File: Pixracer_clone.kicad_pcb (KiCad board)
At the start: 4 copper layers, 47.5 x 47.5 mm, 98 parts, among them J1 Conn_01x03_Male, J10 Conn_01x04_Male, J11 Conn_01x04_Male, J12 Conn_01x04_Male, J13 Conn_01x04_Male, J14 UART4_con, J15 UART4_con, J16 UART4_con, J17 Conn_01x06_Male, J18 Micro_SD_Card, J2 USB_B_Micro, J20 Conn_01x04_Male, J3 Conn_01x08_Male, J4 Conn_01x08_Male, J5 Conn_01x08_Male, J6 Conn_01x02_Male, J7 Conn_01x03_Male, J8 Conn_01x02_Male, J9 UART4_con, Q1 2N3904, Q2 2N3904, SW1 SW_Push, U1 STM32F427VITx, U10 LP5907MFX-3.3, U11 NRF24L01_Breakout, U2 USBLC6-2SC6, U3 ICM-20948, U4 MPU-9250, U5 LSM6DS3, U6 TJA1051T, U7 LP5907MFX-1.8, U8 LP5907MFX-3.3, U9 25LCxxx, Y1 Crystal_GND24

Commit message: finish board
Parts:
- removed C11: 1u, Capacitor_SMD:C_0402_1005Metric
- removed C22: CP, Capacitor_SMD:C_1206_3216Metric
- removed C32: 1uF, Capacitor_SMD:C_0402_1005Metric
- removed C33: 100nF, Capacitor_SMD:C_0402_1005Metric
- removed C41: C, Capacitor_SMD:C_0603_1608Metric
- removed F1: Fuse, Fuse:Fuse_1812_4532Metric
- removed J13: Conn_01x04_Male, Connector_PinHeader_2.54mm:PinHeader_1x04_P2.54mm_Vertical
- removed J9: UART4_con, Connector_PinHeader_2.54mm:PinHeader_1x04_P2.54mm_Vertical
- added C25: CP, Capacitor_SMD:C_1206_3216Metric, F.Cu at (179.1, 112.7)
- added C43: 1uF, Capacitor_SMD:C_0603_1608Metric_Pad1.05x0.95mm_HandSolder, F.Cu at (147.8, 85.1)
- added J19: Conn_01x02_Male, Connector_PinHeader_2.54mm:PinHeader_1x02_P2.54mm_Vertical, F.Cu at (189.6, 88.2)
- added J21: Conn_01x06_Male, Connector_JST:JST_SH_SM06B-SRSS-TB_1x06-1MP_P1.00mm_Horizontal, B.Cu at (147.1, 82.0)
- added J22: Conn_01x06_Male, Connector_JST:JST_SH_SM06B-SRSS-TB_1x06-1MP_P1.00mm_Horizontal, F.Cu at (147.5, 112.7)
- added J23: Conn_01x10_Male, Connector_PinHeader_2.54mm:PinHeader_1x10_P2.54mm_Vertical, F.Cu at (157.6, 120.1)
- added R4: 22R, Resistor_SMD:R_0603_1608Metric_Pad1.05x0.95mm_HandSolder, F.Cu at (185.9, 82.9)
- C15: value C -> 1uF; footprint Capacitor_SMD:C_0603_1608Metric -> Capacitor_SMD:C_0603_1608Metric_Pad1.05x0.95mm_HandSolder
- C39, D2, J8, Q1, R2: moved to B.Cu
- C7, J15, R5, R6, Rc_sbus1: moved to F.Cu
- J14: footprint Connector_JST:JST_SH_BM04B-SRSS-TB_1x04-1MP_P1.00mm_Vertical -> Connector_JST:JST_SH_SM04B-SRSS-TB_1x04-1MP_P1.00mm_Horizontal
- J6: value Conn_01x02_Male -> Conn_01x04_Male; footprint Connector_PinHeader_2.54mm:PinHeader_1x02_P2.54mm_Vertical -> Connector_JST:JST_SH_SM04B-SRSS-TB_1x04-1MP_P1.00mm_Horizontal
- J7: value Conn_01x03_Male -> Conn_01x04_Male; footprint Connector_JST:JST_SH_BM03B-SRSS-TB_1x03-1MP_P1.00mm_Vertical -> Connector_JST:JST_SH_SM04B-SRSS-TB_1x04-1MP_P1.00mm_Horizontal
- R3: value R -> 22R; footprint Resistor_SMD:R_0402_1005Metric -> Resistor_SMD:R_0603_1608Metric_Pad1.05x0.95mm_HandSolder
- U2: value USBLC6-2SC6 -> LP5907MFX-3.3; footprint Package_TO_SOT_SMD:SOT-23-6 -> Package_TO_SOT_SMD:SOT-23-5
- moved C15 67.0 mm to (153.2, 85.1), turned to 90 degrees
- moved R3 55.7 mm to (185.9, 81.2), turned to 180 degrees
- moved C12 48.5 mm to (157.5, 99.4), turned to 90 degrees
- moved C30 41.9 mm to (185.2, 112.7), turned to 90 degrees
- moved J8 39.6 mm to (186.2, 75.8), turned to 90 degrees
- moved C10 39.5 mm to (157.3, 95.6), turned to 90 degrees
- moved C6 39.0 mm to (156.4, 91.8), turned to 90 degrees
- moved Rc_sbus1 38.4 mm to (156.3, 106.9)
- moved J16 35.0 mm to (190.7, 113.9), turned to 90 degrees
- moved U2 34.8 mm to (150.5, 85.2)
- moved R6 32.8 mm to (156.3, 111.1)
- moved Q1 31.8 mm to (184.0, 79.3)
- moved R2 31.6 mm to (187.7, 79.4)
- moved R5 29.8 mm to (156.3, 112.6), turned to 180 degrees
- moved J6 29.4 mm to (162.2, 75.4), turned to 180 degrees
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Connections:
- C15 pad 1: VBUS -> +5V
- C21 pad 1: 5V_IN -> +5V
- C30 pad 1: 5V_IN -> +5V
- D2 pad 1: 5V_IN -> +5V
- J10 pad 2: UART1_RX -> UART1_TX
- J10 pad 3: UART1_TX -> UART1_RX
- J10 pad 4: VCC -> +5V
- J11 pad 4: VCC -> +3V3
- J12 pad 4: VCC -> +5V
- J14 pad 2: I2C_SDA -> I2C_SCl
- J14 pad 3: I2C_SCl -> I2C_SDA
- J14 pad 4: 5V_IN -> +5V
- J15 pad 2: I2C2_SDA -> I2C2_SCl
- J15 pad 3: I2C2_SCl -> I2C2_SDA
- J15 pad 4: 5V_IN -> +5V
- J16 pad 1: VCC -> +5V
- J17 pad 1: VCC -> +5V
- J20 pad 4: 5V_IN -> +5V
- J5 pad 1: 5V_IN -> +5V
- J5 pad 2: 5V_IN -> +5V
- J5 pad 3: 5V_IN -> +5V
- J5 pad 4: 5V_IN -> +5V
- J5 pad 5: 5V_IN -> +5V
- J5 pad 6: 5V_IN -> +5V
- J5 pad 7: 5V_IN -> +5V
- J5 pad 8: 5V_IN -> +5V
- J6 pad 1: Net-(F1-Pad1) -> GND
- J6 pad 2: GND -> UART8_RX
- J7 pad 2: SBUS_DEVICE -> Net-(J7-Pad2)
- J7 pad 3: VCC -> SBUS_DEVICE
- J8 pad 2: 5V_IN -> +5V
- R3 pad 1: +3.3VA -> /USB_sheet/D+
- R3 pad 2: ICM20948_CS -> USB_D+
- R5 pad 1: 5V_IN -> +5V
- Rc_sbus2 pad 2: 5V_IN -> +5V
- U1 pad 3: SPI4_MOSI -> SPI4_CS
- U1 pad 43: Net-(U1-Pad43) -> EXTERNAL_MPU_CS
- U1 pad 51: Net-(U1-Pad51) -> EXTERNAL_MEM_CS
- U1 pad 57: EXTERNAL_MEM_CS -> Net-(U1-Pad57)
- U11 pad 1: Net-(U11-Pad1) -> GND
- U11 pad 2: Net-(U11-Pad2) -> Net-(C43-Pad1)
- U11 pad 3: Net-(U11-Pad3) -> SPI4_CE
- U11 pad 4: Net-(U11-Pad4) -> SPI4_CS
- U11 pad 5: Net-(U11-Pad5) -> SPI4_CLK
- U11 pad 6: Net-(U11-Pad6) -> SPI4_MOSI
- U11 pad 7: Net-(U11-Pad7) -> SPI4_MISO
- U2 pad 1: /USB_sheet/D- -> +5V
- U2 pad 3: /USB_sheet/D+ -> nRF24_EN
- U2 pad 4: USB_D+ -> Net-(U2-Pad4)
- U2 pad 5: VBUS -> Net-(C43-Pad1)
- U6 pad 3: 5V_IN -> +5V
- U8 pad 1: 5V_IN -> +5V
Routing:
- net +5V: track 0.00 -> 179.2 mm, vias 0 -> 19
- net VCC: track 15.1 -> 154.7 mm, vias 4 -> 19
- net GND: track 72.7 -> 133.0 mm, vias 24 -> 77
- net 3.3_SENSE_EN: track 0.00 -> 28.5 mm, vias 0 -> 2
- net UART7_RX: track 0.00 -> 27.7 mm, vias 0 -> 2
- net UART7_TX: track 0.00 -> 27.4 mm, vias 0 -> 2
- net I2C2_SCl: track 0.00 -> 26.2 mm, vias 0 -> 2
- net UART3_TX: track 0.00 -> 25.4 mm, vias 0 -> 2
- net I2C2_SDA: track 0.00 -> 25.0 mm, vias 0 -> 2
- net Buzzer: track 0.00 -> 24.1 mm, vias 0 -> 1
- net SPI3_CS: track 0.00 -> 24.1 mm, vias 0 -> 1
- net nRF24_EN: track 0.00 -> 23.5 mm, vias 0 -> 2
- net SPI3_SCK: track 0.00 -> 23.1 mm, vias 0 -> 1
- net SPI4_MOSI: track 0.00 -> 23.0 mm, vias 0 -> 2
- net UART3_RX: track 0.00 -> 23.0 mm, vias 0 -> 2
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- added copper zone on B.Cu, net GND
- added copper zone on F.Cu, net GND
- added copper zone on In1.Cu, net GND
- added copper zone on In2.Cu, net VCC
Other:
- board size 47.5 x 47.5 mm -> 49.5 x 49.4 mm

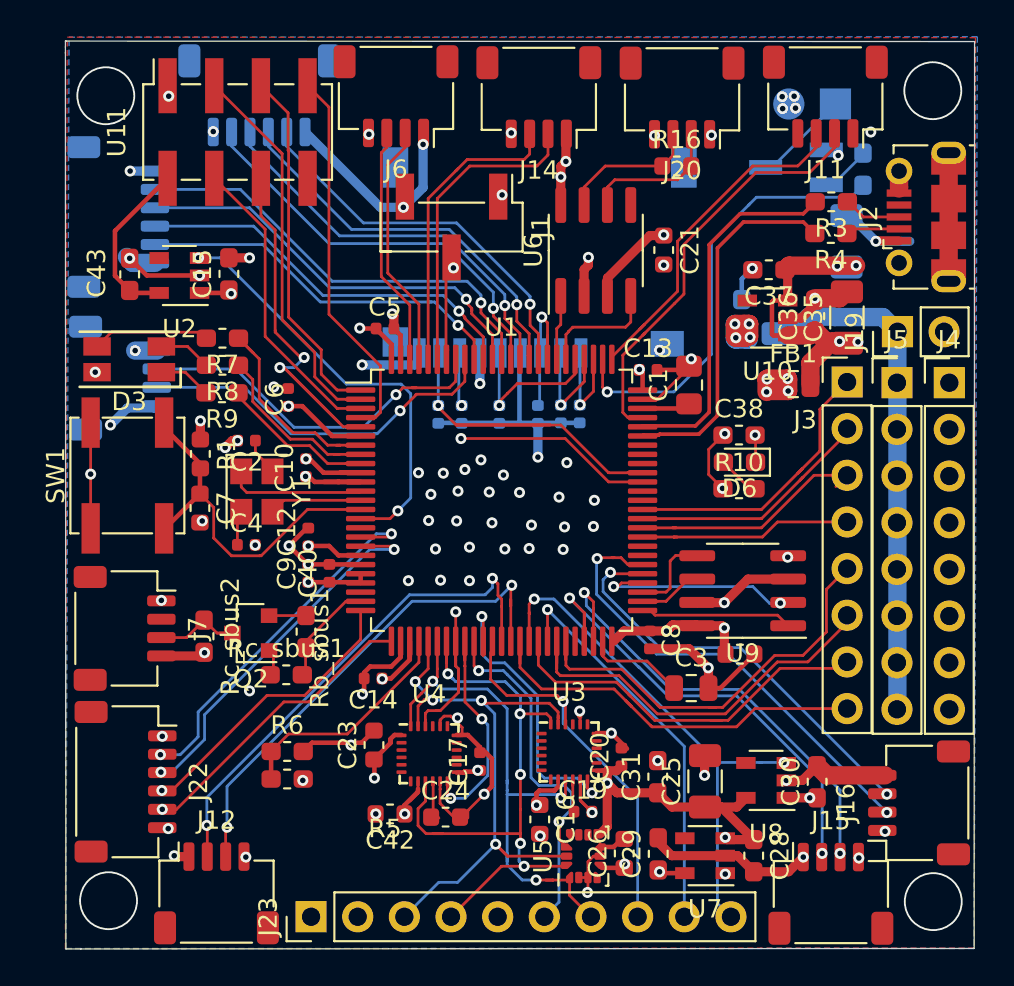
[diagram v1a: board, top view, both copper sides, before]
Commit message: add IMU external board
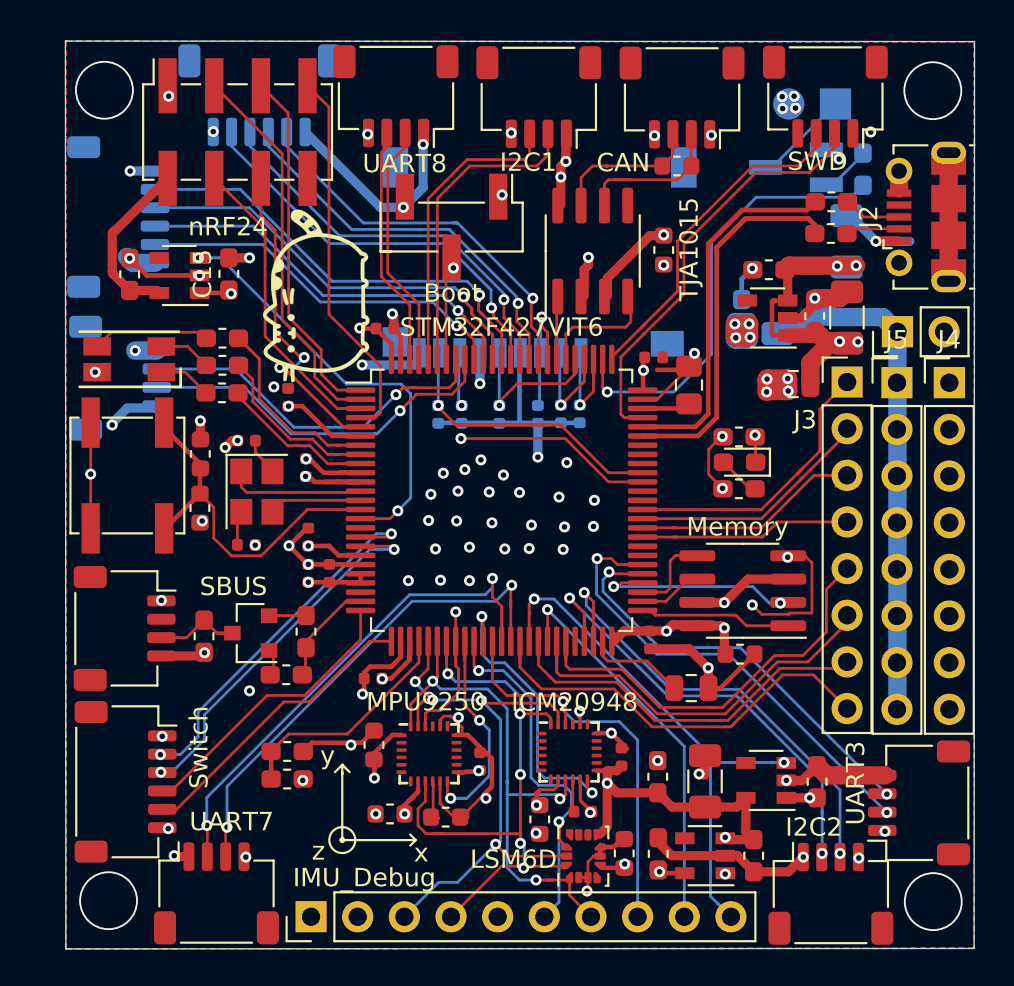
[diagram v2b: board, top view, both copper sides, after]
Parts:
- added G***: LOGO, pusheen:pusheen_small, F.Cu at (157.9, 86.3)
- added G***: LOGO, Pixracer_clone:pusheen, B.Cu at (166.4, 104.4)
- added x: indicator, Pixracer_clone:indicator, F.Cu at (159.3, 115.9)
- moved C13 0.74 mm to (176.3, 89.6)
- moved TJA1015 0.17 mm to (173.0, 83.8)
- moved C38 0.10 mm to (180.9, 94.0)
- renumbered J1 to Boot, J8 to Buzzer, J20 to CAN, J14 to I2C1, J15 to I2C2, U3 to ICM20948, J23 to IMU_Debug, U5 to LSM6D, U4 to MPU9250, U9 to Memory, J7 to SBUS, J18 to SDcard, J21 to SPI3, U1 to STM32F427VIT6, J11 to SWD, J22 to Switch, U6 to TJA1015, J17 to Telemetry, J10 to UART1, J16 to UART3, J12 to UART7, J6 to UART8, U11 to nRF24
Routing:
- net +5V: track 179.2 -> 215.8 mm
- net GND: track 133.0 -> 140.7 mm
- net USB_D-: track 19.8 -> 26.8 mm
- net ICM20948_CS: track 20.6 -> 22.6 mm
- net MPU9250_DRDY: track 13.2 -> 14.9 mm
- net CAN1_TX: track 3.54 -> 5.22 mm
- net TIM1_CH1: track 22.7 -> 24.3 mm
- net 3.3_SENSE_EN: track 28.5 -> 30.0 mm
- net VCC: track 154.7 -> 156.1 mm
- net SDIO_CMD: track 8.16 -> 6.88 mm
- net SWDIO: track 23.1 -> 24.1 mm
- net +3.3VA: track 48.9 -> 48.0 mm
- net USB_D+: track 19.9 -> 20.7 mm
- net UART3_TX: track 25.4 -> 26.2 mm
- net IMU_MISO: track 29.7 -> 30.4 mm
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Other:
- outline, holes or cut-outs redrawn
- net class USB added: clearance 0.2032, trace_width 0.1524, via_dia 0.6, via_drill 0.3
